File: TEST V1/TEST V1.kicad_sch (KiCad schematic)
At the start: 107 parts, among them IC1 W25Q16JVUXIQ, J1 Conn_01x02_Pin, J10 Conn_01x03_Socket, J3 DIN41612_02x08_AB_EvenPins, J4 Conn_01x02_Pin, J9 USB_C_Receptacle_USB2.0_14P, SW1 SW_Push_Dual, SW2 SW_Push_Dual, U1 AD9833, U10 MCP4725A2T-ECH, U11 74AHCT125, U12 SN74LVC244APWT, U2 MCP4725A2T-ECH, U3 LM318N, U4 LM318N, U5 RP2040, U6 TPS54202DDC, U7 MCP4725A2T-ECH, U8 MCP4725A2T-ECH, Y1 25 MHz, Y2 Crystal_12MHz

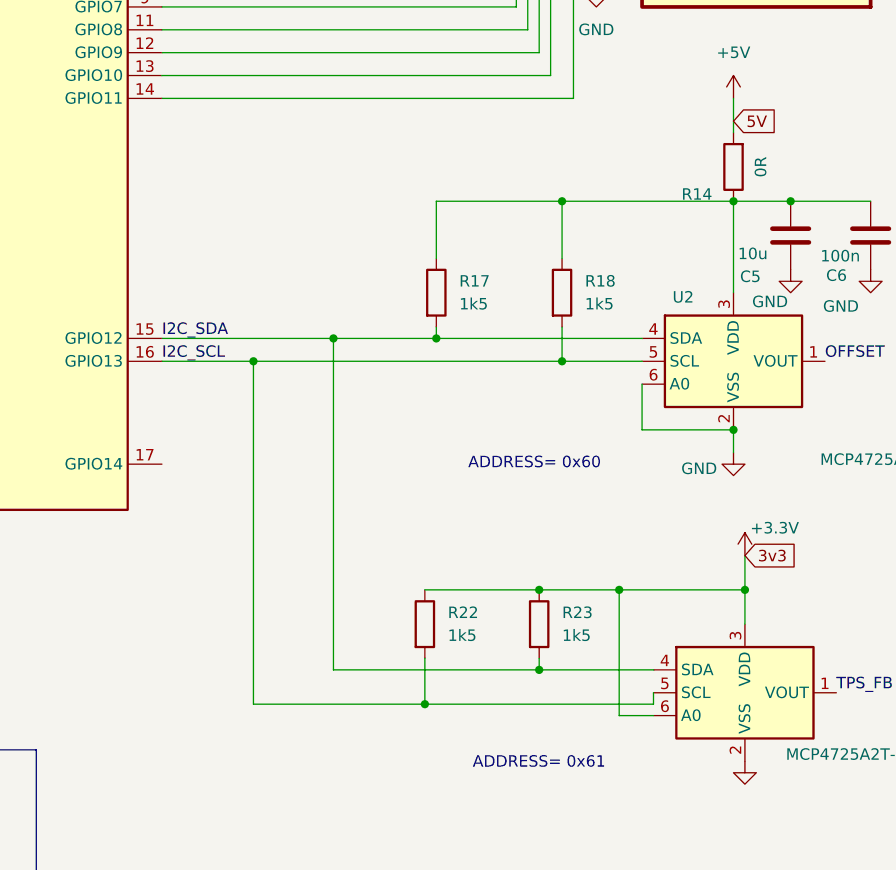
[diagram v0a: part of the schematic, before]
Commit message: i2c schematic correction done
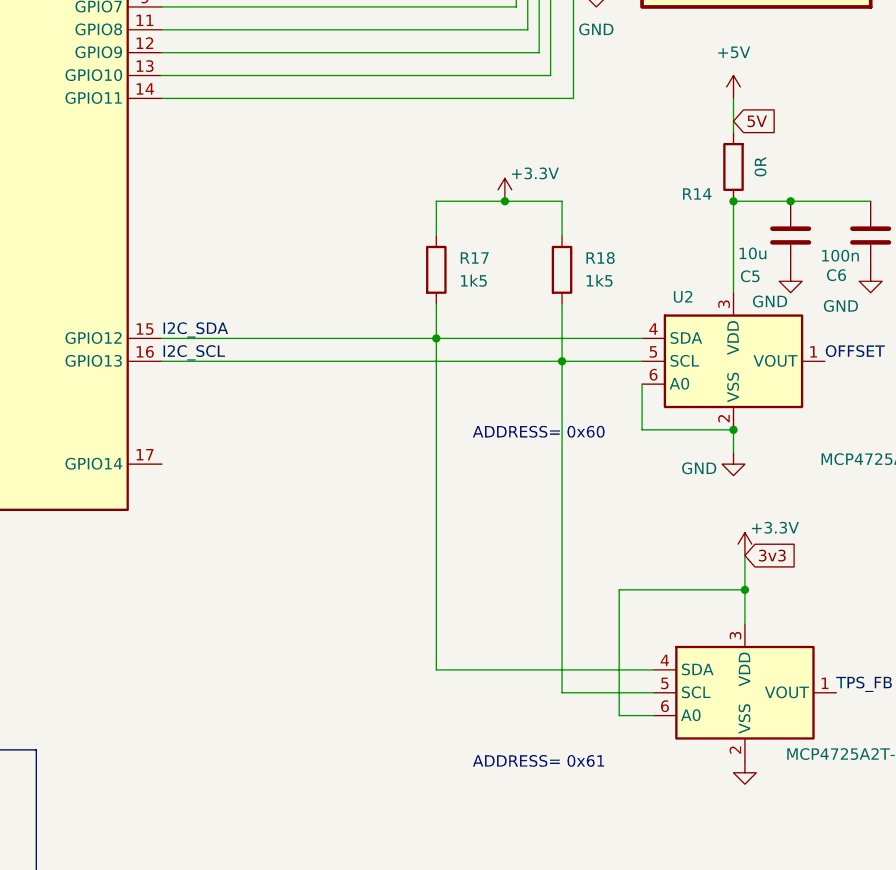
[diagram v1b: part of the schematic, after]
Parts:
- removed R22, R23: 1k5, symbol Device:R
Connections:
- net +3.3V: now also R17.1, R18.1
- net at C5.2, C6.2, R14.1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: no longer R17.1, R18.1

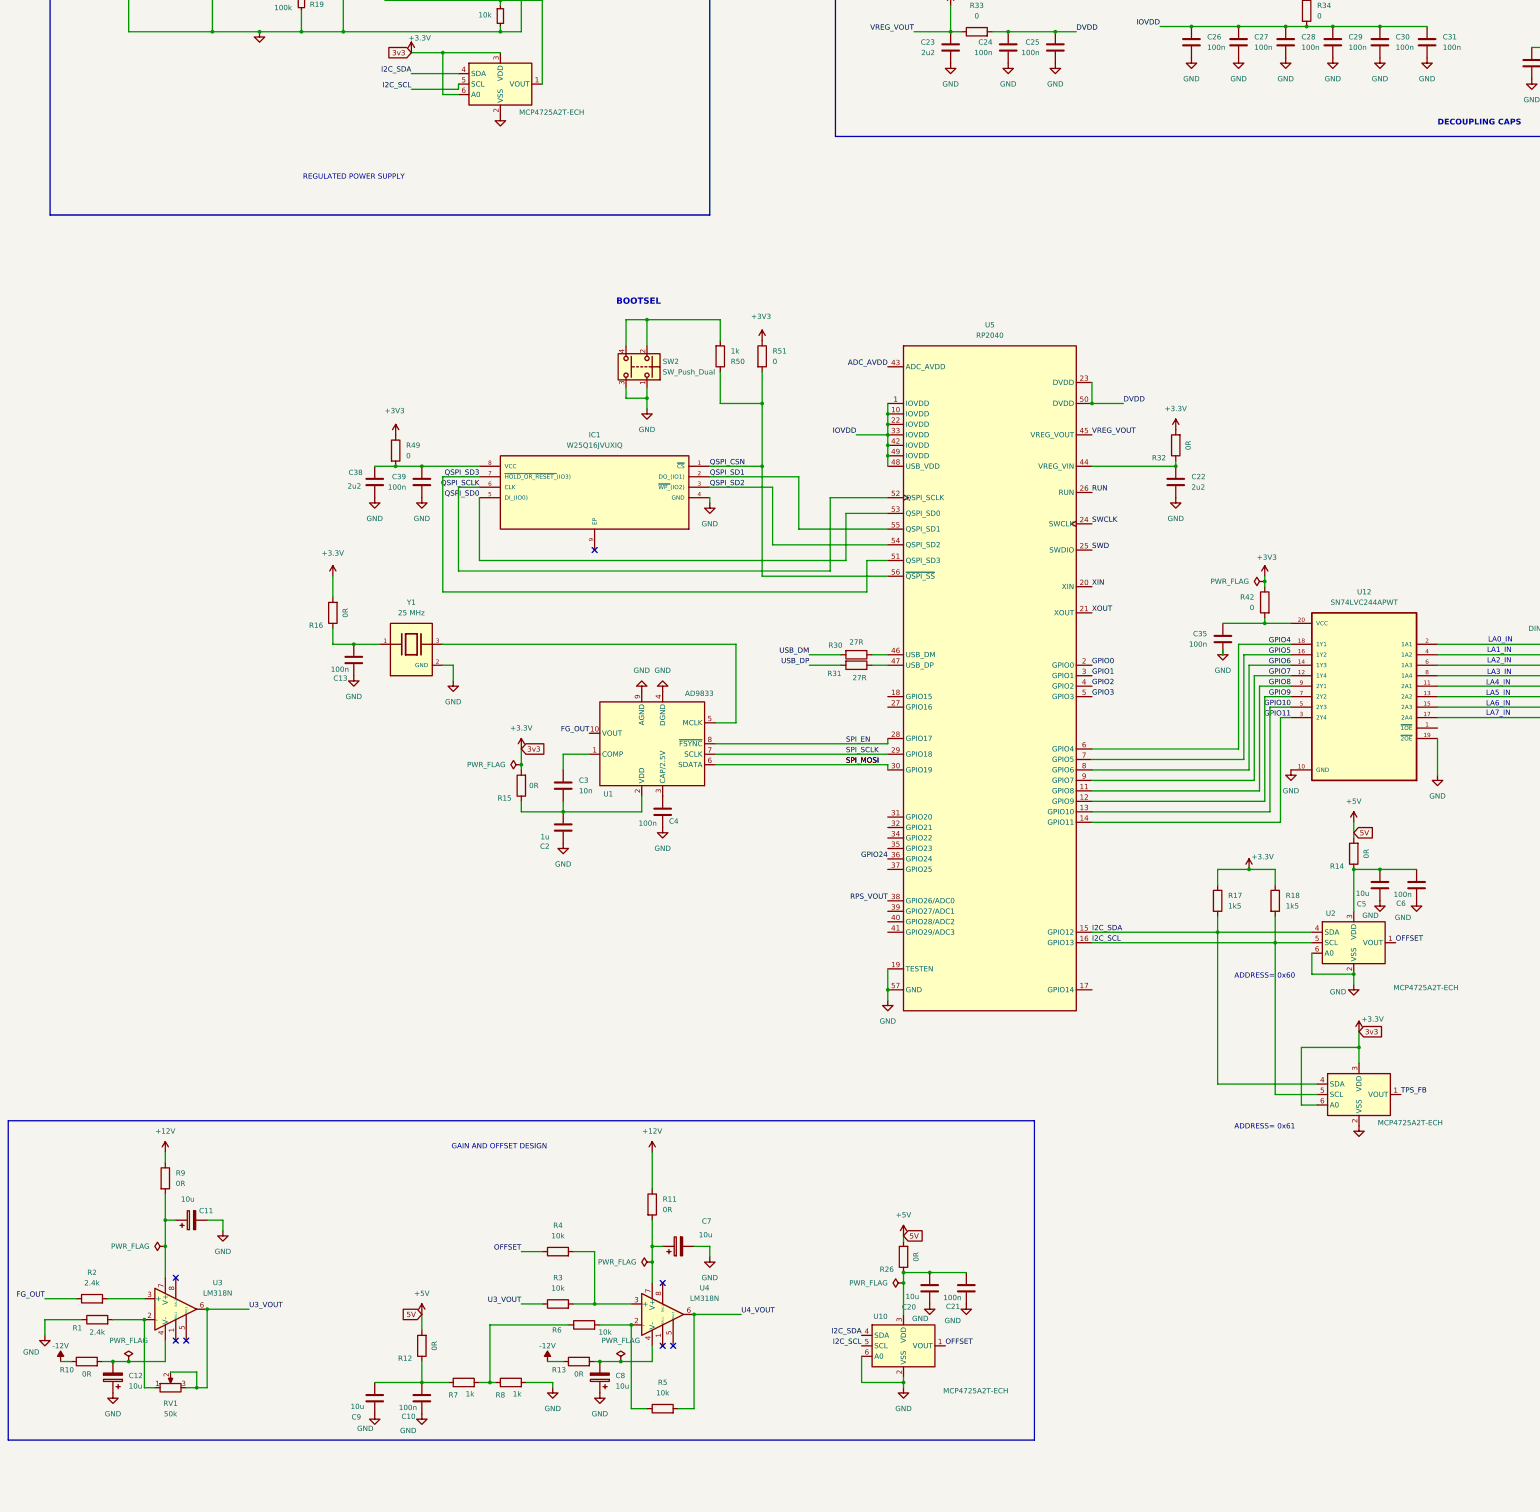
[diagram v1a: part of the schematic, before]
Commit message: added hierarchical sheets
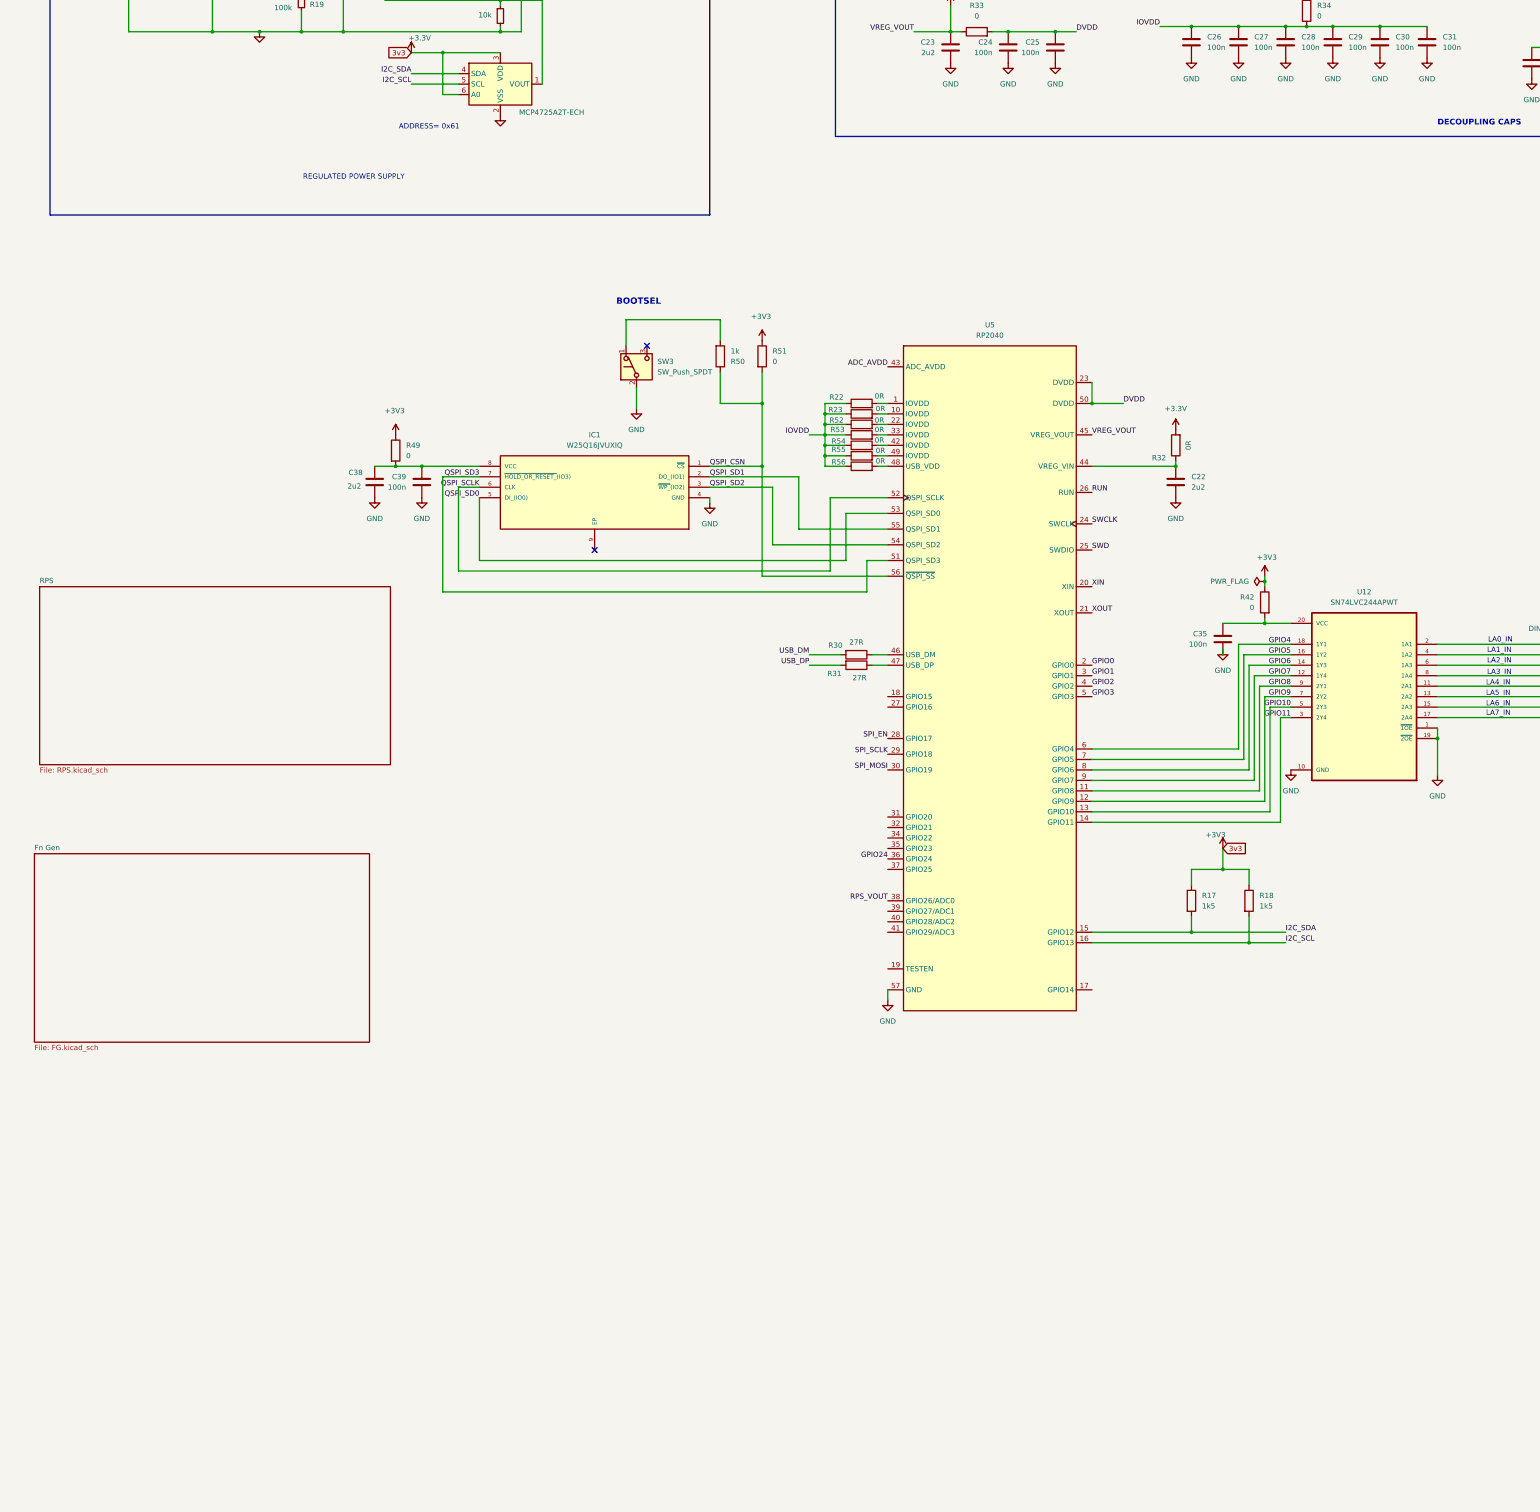
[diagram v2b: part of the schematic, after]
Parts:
- removed C10, C13, C21, C4, C6: 100n, symbol Device:C
- removed C11, C12, C7, C8: 10u, symbol Device:C_Polarized
- removed C2: 1u, symbol Device:C
- removed C20, C5, C9: 10u, symbol Device:C
- removed C3: 10n, symbol Device:C
- removed R1, R2: 2.4k, symbol Device:R
- removed R10, R11, R12, R13, R14, R15, R16, R26, R9: 0R, symbol Device:R
- removed R3, R4, R5, R6: 10k, symbol Device:R
- removed R7, R8: 1k, symbol Device:R
- removed RV1: 50k, symbol Device:R_Potentiometer
- removed SW2: SW_Push_Dual, Button_Switch_THT:SW_Push_2P1T_Toggle_CK_PVA1xxH1xxxxxxV2, symbol Switch:SW_Push_Dual
- removed U1: AD9833, Package_SO:MSOP-10_3x3mm_P0.5mm, symbol Interface:AD9833xRM
- removed U10, U2, U8: MCP4725A2T-ECH, Package_TO_SOT_SMD:SOT-23-6, symbol Analog_DAC:MCP4725xxx-xCH
- removed U3, U4: LM318N, symbol Amplifier_Operational:LM318N
- removed Y1: 25 MHz, C3E-16.000-12-1015-X-M:XTAL_C3E-16.000-12-1015-X-M, symbol C3E-16.000-12-1015-X-M:C3E-16.000-12-1015-X-M
- added R22, R23, R52, R53, R54, R55, R56: 0R, symbol Device:R
- added SW3: SW_Push_SPDT, symbol Switch:SW_Push_SPDT
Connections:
- net +3V3 is gone; now on net +3.3V: R34.1, R35.1, R42.1, R45.1, R49.1, R51.1
- net GND: now also U12.1 (~{1OE}), SW3.2 (B); no longer U5.19 (TESTEN)
- net IOVDD: now also R22.1, R23.1, R52.1, R53.1, R54.1, R55.1, R56.1; no longer U5.1 (IOVDD), U5.10 (IOVDD), U5.22 (IOVDD), U5.33 (IOVDD), U5.42 (IOVDD), U5.48 (USB_VDD), U5.49 (IOVDD)
- net at R50.2: now also SW3.1 (A)
- new net: R52.2, U5.22 (IOVDD)
- new net: R53.2, U5.33 (IOVDD)
- new net: R54.2, U5.42 (IOVDD)
- new net: R56.2, U5.48 (USB_VDD)
- new net: R23.2, U5.10 (IOVDD)
- new net: R22.2, U5.1 (IOVDD)
- new net: R55.2, U5.49 (IOVDD)
- no-connect marks 10 -> 5
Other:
- added sheet Fn Gen (FG.kicad_sch)
- added sheet RPS (RPS.kicad_sch)
- note removed: "ADDRESS= 0x60"
- note removed: "GAIN AND OFFSET DESIGN"
- moved on the sheet: R17, R18

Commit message: Integrated FG, RPS, and PCB updates
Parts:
- removed C1: 100n, Capacitor_THT:C_Disc_D5.0mm_W2.5mm_P5.00mm, symbol Device:C_Small
- removed C14: 10u, Capacitor_THT:C_Disc_D6.0mm_W4.4mm_P5.00mm, symbol Device:C_Small
- removed C15: 0.1u, Capacitor_THT:C_Disc_D5.0mm_W2.5mm_P5.00mm, symbol Device:C_Small
- removed C16, C17: 22u, Capacitor_THT:C_Disc_D6.0mm_W4.4mm_P5.00mm, symbol Device:C_Small
- removed J1: Conn_01x02_Pin, Connector_PinHeader_2.54mm:PinHeader_1x01_P2.54mm_Horizontal, symbol Connector:Conn_01x02_Pin
- removed J2: ~, Connector_PinHeader_2.54mm:PinHeader_1x01_P2.54mm_Vertical, symbol Connector:Conn_01x01_Pin
- removed J3: DIN41612_02x08_AB_EvenPins, Connector_PinHeader_2.00mm:PinHeader_2x08_P2.00mm_Horizontal, symbol Connector:DIN41612_02x08_AB_EvenPins
- removed J4: Conn_01x02_Pin, symbol Connector:Conn_01x02_Pin
- removed L1: 16u, Inductor_THT:L_Radial_D8.7mm_P5.00mm_Fastron_07HCP, symbol Device:L_Iron_Small
- removed R19: 100k, Resistor_SMD:R_0805_2012Metric_Pad1.20x1.40mm_HandSolder, symbol Device:R_Small
- removed R20: 190k, Resistor_SMD:R_0805_2012Metric_Pad1.20x1.40mm_HandSolder, symbol Device:R_Small
- removed R21: 10k, Resistor_SMD:R_0805_2012Metric_Pad1.20x1.40mm_HandSolder, symbol Device:R_Small
- removed SW1: SW_Push_Dual, Button_Switch_THT:SW_Push_2P1T_Toggle_CK_PVA1xxH1xxxxxxV2, symbol Switch:SW_Push_Dual
- removed U6: TPS54202DDC, Package_TO_SOT_SMD:SOT-23-6, symbol Regulator_Switching:TPS54202DDC
- removed U7: MCP4725A2T-ECH, Package_TO_SOT_SMD:SOT-23-6, symbol Analog_DAC:MCP4725xxx-xCH
- added J1: Conn_01x16_Socket, Connector_PinHeader_2.54mm:PinHeader_1x16_P2.54mm_Horizontal, symbol Connector:Conn_01x16_Socket
- added R4: 10k, Resistor_SMD:R_0603_1608Metric_Pad0.98x0.95mm_HandSolder, symbol Device:R
- added SW2: SW_Push_SPDT, symbol Switch:SW_Push_SPDT
- C1: renamed from C38; footprint Capacitor_SMD:C_1206_3216Metric_Pad1.33x1.80mm_HandSolder -> Capacitor_SMD:C_0603_1608Metric_Pad1.08x0.95mm_HandSolder
- C10: renamed from C28; footprint Capacitor_SMD:C_1206_3216Metric_Pad1.33x1.80mm_HandSolder -> Capacitor_SMD:C_0603_1608Metric_Pad1.08x0.95mm_HandSolder
- C11: renamed from C29; footprint Capacitor_SMD:C_1206_3216Metric_Pad1.33x1.80mm_HandSolder -> Capacitor_SMD:C_0603_1608Metric_Pad1.08x0.95mm_HandSolder
- C12: renamed from C30; footprint Capacitor_SMD:C_1206_3216Metric_Pad1.33x1.80mm_HandSolder -> Capacitor_SMD:C_0603_1608Metric_Pad1.08x0.95mm_HandSolder
- C13: renamed from C31; footprint Capacitor_SMD:C_1206_3216Metric_Pad1.33x1.80mm_HandSolder -> Capacitor_SMD:C_0603_1608Metric_Pad1.08x0.95mm_HandSolder
- C14: renamed from C32; footprint Capacitor_SMD:C_1206_3216Metric_Pad1.33x1.80mm_HandSolder -> Capacitor_SMD:C_0603_1608Metric_Pad1.08x0.95mm_HandSolder
- C15: renamed from C33; footprint Capacitor_SMD:C_1206_3216Metric_Pad1.33x1.80mm_HandSolder -> Capacitor_SMD:C_0603_1608Metric_Pad1.08x0.95mm_HandSolder
- C16: renamed from C36; footprint Capacitor_SMD:C_1206_3216Metric_Pad1.33x1.80mm_HandSolder -> Capacitor_SMD:C_0603_1608Metric_Pad1.08x0.95mm_HandSolder
- C17: renamed from C37; footprint Capacitor_SMD:C_1206_3216Metric_Pad1.33x1.80mm_HandSolder -> Capacitor_SMD:C_0603_1608Metric_Pad1.08x0.95mm_HandSolder
- C18: renamed from C34; footprint Capacitor_SMD:C_1206_3216Metric_Pad1.33x1.80mm_HandSolder -> Capacitor_SMD:C_0603_1608Metric_Pad1.08x0.95mm_HandSolder
- C2: renamed from C39; footprint Capacitor_SMD:C_1206_3216Metric_Pad1.33x1.80mm_HandSolder -> Capacitor_SMD:C_0603_1608Metric_Pad1.08x0.95mm_HandSolder
- C3: renamed from C23; footprint Capacitor_SMD:C_1206_3216Metric_Pad1.33x1.80mm_HandSolder -> Capacitor_SMD:C_0603_1608Metric_Pad1.08x0.95mm_HandSolder
- C4: renamed from C24; footprint Capacitor_SMD:C_1206_3216Metric_Pad1.33x1.80mm_HandSolder -> Capacitor_SMD:C_0603_1608Metric_Pad1.08x0.95mm_HandSolder
- C5: renamed from C25; footprint Capacitor_SMD:C_1206_3216Metric_Pad1.33x1.80mm_HandSolder -> Capacitor_SMD:C_0603_1608Metric_Pad1.08x0.95mm_HandSolder
- C6: renamed from C22; footprint (none) -> Capacitor_SMD:C_0603_1608Metric_Pad1.08x0.95mm_HandSolder
- C7: renamed from C26; footprint Capacitor_SMD:C_1206_3216Metric_Pad1.33x1.80mm_HandSolder -> Capacitor_SMD:C_0603_1608Metric_Pad1.08x0.95mm_HandSolder
- C8: renamed from C27; footprint Capacitor_SMD:C_1206_3216Metric_Pad1.33x1.80mm_HandSolder -> Capacitor_SMD:C_0603_1608Metric_Pad1.08x0.95mm_HandSolder
- C9: renamed from C35; footprint Capacitor_SMD:C_1206_3216Metric_Pad1.33x1.80mm_HandSolder -> Capacitor_SMD:C_0603_1608Metric_Pad1.08x0.95mm_HandSolder
- R1: renamed from R49; footprint Resistor_SMD:R_1206_3216Metric_Pad1.30x1.75mm_HandSolder -> Resistor_SMD:R_0603_1608Metric_Pad0.98x0.95mm_HandSolder
- R10: renamed from R53; footprint (none) -> Resistor_SMD:R_0603_1608Metric_Pad0.98x0.95mm_HandSolder
- R11: renamed from R54; footprint (none) -> Resistor_SMD:R_0603_1608Metric_Pad0.98x0.95mm_HandSolder
- R12: renamed from R55; footprint (none) -> Resistor_SMD:R_0603_1608Metric_Pad0.98x0.95mm_HandSolder
- R13: renamed from R56; footprint (none) -> Resistor_SMD:R_0603_1608Metric_Pad0.98x0.95mm_HandSolder
- R14: renamed from R33; footprint Resistor_SMD:R_1206_3216Metric_Pad1.30x1.75mm_HandSolder -> Resistor_SMD:R_0603_1608Metric_Pad0.98x0.95mm_HandSolder
- R15: renamed from R32; footprint (none) -> Resistor_SMD:R_0603_1608Metric_Pad0.98x0.95mm_HandSolder
- R16: renamed from R17; footprint (none) -> Resistor_SMD:R_0603_1608Metric_Pad0.98x0.95mm_HandSolder
- R17: renamed from R18; footprint (none) -> Resistor_SMD:R_0603_1608Metric_Pad0.98x0.95mm_HandSolder
- R18: renamed from R34; footprint Resistor_SMD:R_1206_3216Metric_Pad1.30x1.75mm_HandSolder -> Resistor_SMD:R_0603_1608Metric_Pad0.98x0.95mm_HandSolder
- R19: renamed from R42; footprint Resistor_SMD:R_1206_3216Metric_Pad1.30x1.75mm_HandSolder -> Resistor_SMD:R_0603_1608Metric_Pad0.98x0.95mm_HandSolder
- R2: renamed from R50; footprint Resistor_SMD:R_1206_3216Metric_Pad1.30x1.75mm_HandSolder -> Resistor_SMD:R_0603_1608Metric_Pad0.98x0.95mm_HandSolder
- R20: renamed from R35; footprint Resistor_SMD:R_1206_3216Metric_Pad1.30x1.75mm_HandSolder -> Resistor_SMD:R_0603_1608Metric_Pad0.98x0.95mm_HandSolder
- R21: renamed from R36; footprint Resistor_SMD:R_1206_3216Metric_Pad1.30x1.75mm_HandSolder -> Resistor_SMD:R_0603_1608Metric_Pad0.98x0.95mm_HandSolder
- R22: renamed from R38; footprint Resistor_SMD:R_1206_3216Metric_Pad1.30x1.75mm_HandSolder -> Resistor_SMD:R_0603_1608Metric_Pad0.98x0.95mm_HandSolder
- R23: renamed from R39; footprint Resistor_SMD:R_1206_3216Metric_Pad1.30x1.75mm_HandSolder -> Resistor_SMD:R_0603_1608Metric_Pad0.98x0.95mm_HandSolder
- R24: renamed from R40; footprint Resistor_SMD:R_1206_3216Metric_Pad1.30x1.75mm_HandSolder -> Resistor_SMD:R_0603_1608Metric_Pad0.98x0.95mm_HandSolder
- R25: renamed from R41; footprint Resistor_SMD:R_1206_3216Metric_Pad1.30x1.75mm_HandSolder -> Resistor_SMD:R_0603_1608Metric_Pad0.98x0.95mm_HandSolder
- R26: renamed from R43; footprint Resistor_SMD:R_1206_3216Metric_Pad1.30x1.75mm_HandSolder -> Resistor_SMD:R_0603_1608Metric_Pad0.98x0.95mm_HandSolder
- R27: renamed from R44; footprint Resistor_SMD:R_1206_3216Metric_Pad1.30x1.75mm_HandSolder -> Resistor_SMD:R_0603_1608Metric_Pad0.98x0.95mm_HandSolder
- R28: renamed from R45; footprint Resistor_SMD:R_0402_1005Metric_Pad0.72x0.64mm_HandSolder -> Resistor_SMD:R_0603_1608Metric_Pad0.98x0.95mm_HandSolder
- R29: renamed from R46; footprint Resistor_SMD:R_1206_3216Metric_Pad1.30x1.75mm_HandSolder -> Resistor_SMD:R_0603_1608Metric_Pad0.98x0.95mm_HandSolder
- R3: renamed from R51; footprint Resistor_SMD:R_1206_3216Metric_Pad1.30x1.75mm_HandSolder -> Resistor_SMD:R_0603_1608Metric_Pad0.98x0.95mm_HandSolder
- R30: renamed from R47; footprint Resistor_SMD:R_1206_3216Metric_Pad1.30x1.75mm_HandSolder -> Resistor_SMD:R_0603_1608Metric_Pad0.98x0.95mm_HandSolder
- R31: renamed from R37; footprint Resistor_SMD:R_1206_3216Metric_Pad1.30x1.75mm_HandSolder -> Resistor_SMD:R_0603_1608Metric_Pad0.98x0.95mm_HandSolder
- R32: renamed from R48; footprint Resistor_SMD:R_1206_3216Metric_Pad1.30x1.75mm_HandSolder -> Resistor_SMD:R_0603_1608Metric_Pad0.98x0.95mm_HandSolder
- R5: renamed from R30; footprint (none) -> Resistor_SMD:R_0603_1608Metric_Pad0.98x0.95mm_HandSolder
- R6: renamed from R31; footprint (none) -> Resistor_SMD:R_0603_1608Metric_Pad0.98x0.95mm_HandSolder
- R7: renamed from R22; footprint (none) -> Resistor_SMD:R_0603_1608Metric_Pad0.98x0.95mm_HandSolder
- R8: renamed from R23; footprint (none) -> Resistor_SMD:R_0603_1608Metric_Pad0.98x0.95mm_HandSolder
- R9: renamed from R52; footprint (none) -> Resistor_SMD:R_0603_1608Metric_Pad0.98x0.95mm_HandSolder
- renumbered J9 to J2, J10 to J3, SW3 to SW1, U5 to U1, U12 to U2, U11 to U3, Y2 to Y1
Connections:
- net +3.3V: now also J1.15 (Pin_15)
- net GND: now also J1.16 (Pin_16), SW2.2 (B)
- net QSPI_CSN: now also R4.2; no longer R3.2
- net RUN: now also SW2.3 (C)
- net PG0_OUT: now reaches R22.2
- net PG0_OUT: now also J1.9 (Pin_9)
- net PG1_OUT: now reaches R23.2
- net PG1_OUT: now also J1.10 (Pin_10)
- net PG2_OUT: now reaches R24.2
- net PG2_OUT: now also J1.11 (Pin_11)
- net PG3_OUT: now reaches R25.2
- net PG3_OUT: now also J1.12 (Pin_12)
- net LA4_IN: now reaches U2.11 (2A1)
- net LA4_IN: now also J1.5 (Pin_5)
- net LA5_IN: now reaches U2.13 (2A2)
- net LA5_IN: now also J1.6 (Pin_6)
- net LA6_IN: now reaches U2.15 (2A3)
- net LA6_IN: now also J1.7 (Pin_7)
- net LA7_IN: now reaches U2.17 (2A4)
- net LA7_IN: now also J1.8 (Pin_8)
- net LA0_IN: now reaches U2.2 (1A1)
- net LA0_IN: now also J1.1 (Pin_1)
- net LA1_IN: now reaches U2.4 (1A2)
- net LA1_IN: now also J1.2 (Pin_2)
- net LA2_IN: now reaches U2.6 (1A3)
- net LA2_IN: now also J1.3 (Pin_3)
- net LA3_IN: now reaches U2.8 (1A4)
- net LA3_IN: now also J1.4 (Pin_4)
- new net: R3.2, R4.1
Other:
- note removed: "ADDRESS= 0x61"
- note removed: "LA0_IN"
- note removed: "LA1_IN"
- note removed: "LA2_IN"
- note removed: "LA3_IN"
- note removed: "LA4_IN"
- note removed: "LA5_IN"
- note removed: "LA6_IN"
- note removed: "LA7_IN"
- note removed: "PG0_OUT"
- note removed: "PG1_OUT"
- note removed: "PG2_OUT"
- note removed: "PG3_OUT"
- note removed: "REGULATED POWER SUPPLY"
- moved on the sheet: C18, C9, R16, R17, R19, R2, R22, R23, R24, R25, R3, R31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
